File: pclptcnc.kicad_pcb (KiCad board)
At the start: 2 copper layers, 175.3 x 61 mm, 250 parts, among them P1 ARK825A-3, P3 ARK825A-4, P4 ARK825A-3, P5 ARK825A-3, P6 ARK825A-3, P7 ARK825A-3, P8 ARK825A-3, Q1 BC807-40, Q10 BC807-40, Q11 BC807-40, Q12 BC807-40, Q13 BC807-40, Q14 BC807-40, Q15 BC807-40, Q16 BC807-40, Q17 BC807-40, Q18 BC807-40, Q2 BC807-40, Q3 BC807-40, Q4 BC807-40, Q5 BC807-40, Q6 BC807-40, Q7 BC807-40, Q8 BC807-40, Q9 BC807-40, U1 74LVC1G3157GW, U10 SN74LVC2G17, U11 74HCT14, U12 SN74LVC2G17, U13 74HCT14, U2 HCPL2630, U3 HCPL2630, U4 HCPL2630, U5 HCPL2630, U6 HCPL2630, U7 HCPL2630, U8 74HCT14, U9 74HCT14, j1 DB25, j2 DB25

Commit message: working on
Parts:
- CU1: moved to B.Cu
- moved H3 64.8 mm to (-15.4, 89.5)
- moved C2 54.4 mm to (-1.02, 49.1)
- moved C3 54.4 mm to (-4.95, 49.1)
- moved C4 54.4 mm to (-2.98, 49.1)
- moved D1 54.4 mm to (-6.92, 49.1)
- moved R_LED2 54.4 mm to (-6.92, 45.8)
- moved H4 53.7 mm to (215.7, 75.6)
- moved C7 53.0 mm to (-2.10, 102.0)
- moved C8 53.0 mm to (-0.13, 102.0)
- moved C6 53.0 mm to (-4.06, 102.0)
- moved D14 53.0 mm to (-6.03, 102.0)
- moved R_LED15 53.0 mm to (-6.03, 98.6)
- moved F2 52.0 mm to (16.5, 55.9)
- moved DC/DC1 48.5 mm to (0.00, 64.8), turned to 270 degrees
- moved P1 45.5 mm to (44.3, 92.1)
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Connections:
- C1 pad 1: VCC -> /ISOLATED_VCC
- C1 pad 2: GND -> /ISOLATED_GND
- C2 pad 1: VCC -> /ISOLATED_VCC
- C2 pad 2: GND -> /ISOLATED_GND
- C3 pad 1: VCC -> /ISOLATED_VCC
- C3 pad 2: GND -> /ISOLATED_GND
- C4 pad 1: VCC -> /ISOLATED_VCC
- C4 pad 2: GND -> /ISOLATED_GND
- C5 pad 1: /ISOLATED_VCC -> VCC
- C5 pad 2: /ISOLATED_GND -> GND
- C6 pad 1: /ISOLATED_VCC -> VCC
- C6 pad 2: /ISOLATED_GND -> GND
- C7 pad 1: /ISOLATED_VCC -> VCC
- C7 pad 2: /ISOLATED_GND -> GND
- C8 pad 1: /ISOLATED_VCC -> VCC
- C8 pad 2: /ISOLATED_GND -> GND
- D1 pad 1: VCC -> /ISOLATED_VCC
- D14 pad 1: /ISOLATED_VCC -> VCC
- DC/DC1 pad 5: /ISOLATED_GND -> GND
- DC/DC1 pad 7: /ISOLATED_VCC_NFused -> /VCC_NFused
- F1 pad 1: /VCC_NFused -> /ISOLATED_VCC_NFused
- F1 pad 2: VCC -> /ISOLATED_VCC
- F2 pad 1: /ISOLATED_VCC_NFused -> /VCC_NFused
- F2 pad 2: /ISOLATED_VCC -> VCC
- P1 pad 1: /VCC_NFused -> /ISOLATED_VCC_NFused
- P1 pad 3: GND -> /ISOLATED_GND
- R_LED15 pad 1: /ISOLATED_GND -> GND
- R_LED2 pad 2: GND -> /ISOLATED_GND
- TVS1 pad 1: GND -> /ISOLATED_GND
- TVS1 pad 2: VCC -> /ISOLATED_VCC
- TVS2 pad 1: /ISOLATED_GND -> GND
- TVS2 pad 2: /ISOLATED_VCC -> VCC
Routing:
- net GND: track 472.9 -> 56.7 mm, vias 42 -> 7
- net VCC: track 314.8 -> 219.3 mm, vias 11 -> 10
- net /PC8: track 57.7 -> 6.46 mm
- net /PC5: track 53.3 -> 4.42 mm
- net /PC10: track 37.4 -> 21.9 mm
- net /PC7: track 18.6 -> 3.28 mm
- net /PC4: track 16.4 -> 2.27 mm
- net /PC3: track 15.6 -> 1.76 mm
- net /ISOLATED_GND: track 36.8 -> 24.2 mm
- net /PC6: track 14.6 -> 2.39 mm
- net /PC1: track 13.3 -> 2.81 mm
- net /PC2: track 18.2 -> 8.56 mm
- net /PC_OUT_A6: track 73.5 -> 64.6 mm
- net /PC_OUT_A9: track 56.9 -> 50.0 mm
- net /PC_OUT_A5: track 71.9 -> 66.7 mm
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- removed copper zone on F.Cu, net /ISOLATED_VCC
- removed copper zone on F.Cu, net /ISOLATED_VCC_NFused
- removed copper zone on F.Cu, net /VCC_NFused
- removed copper zone on F.Cu, net VCC
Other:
- board size 175.3 x 61 mm -> 174.8 x 59.1 mm

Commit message: regular
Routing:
- net /PC2: track 8.56 -> 1.38 mm
- net VCC: track 219.3 -> 215.9 mm
- net /PC_OUT_A8: track 59.4 -> 56.2 mm
- net /PC_OUT_A7: track 63.7 -> 61.3 mm
- net /PC_OUT_A3: track 2.79 -> 4.80 mm
- net /PC_OUT_A11: track 2.79 -> 4.75 mm
- net /PC_OUT_A2: track 2.79 -> 4.70 mm
- net /PC1: track 2.81 -> 1.38 mm
- net /PC_OUT_A4: track 67.1 -> 65.9 mm
- net /PC_OUT_A5: track 66.7 -> 65.7 mm
- net /PC_OUT_A6: track 64.6 -> 65.6 mm
- net /PC4: track 2.27 -> 1.38 mm

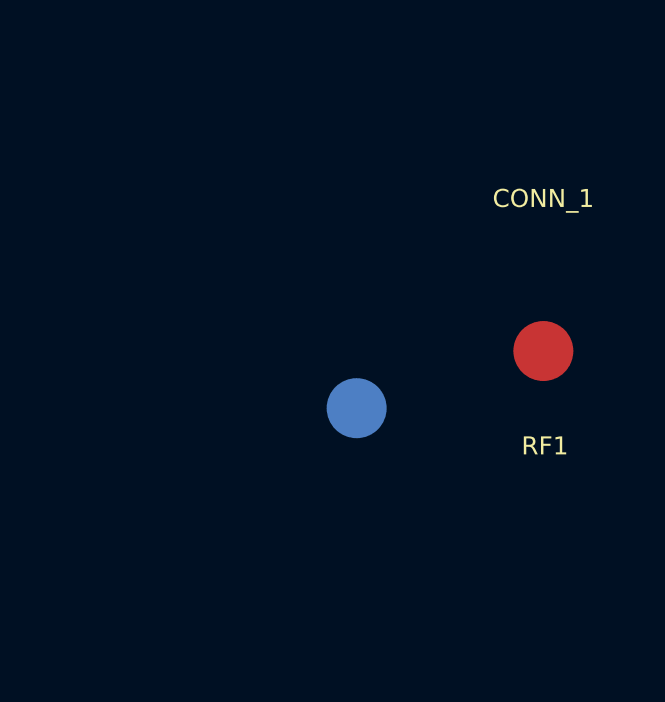
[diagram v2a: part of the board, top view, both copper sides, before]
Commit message: merged all libraries
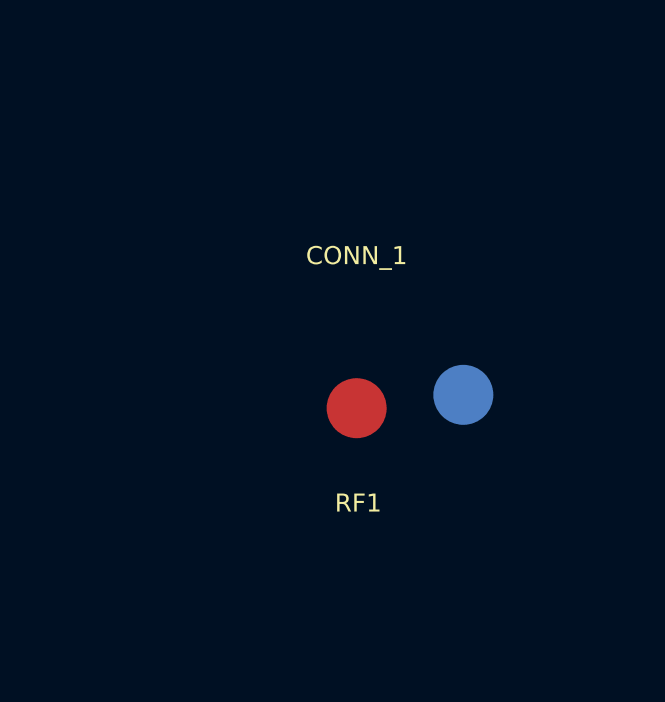
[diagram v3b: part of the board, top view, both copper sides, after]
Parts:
- moved RF1 6.51 mm to (222.1, 52.7)
- moved RF1 3.58 mm to (225.6, 52.3)
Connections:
- DC/DC1 pad 7: /VCC_NFused -> (no net)
- MUX1 pad 10: /PC4 -> (no net)
- MUX1 pad 11: /RC4 -> /PC4
- MUX1 pad 13: /PC3 -> (no net)
- MUX1 pad 14: /RC3 -> (no net)
- MUX1 pad 2: /RC2 -> (no net)
- MUX1 pad 3: /PC2 -> (no net)
- MUX2 pad 10: /PC8 -> (no net)
- MUX2 pad 11: /RC8 -> /PC8
- MUX2 pad 13: /PC7 -> (no net)
- MUX2 pad 14: /RC7 -> (no net)
- MUX2 pad 2: /RC6 -> (no net)
- MUX2 pad 3: /PC6 -> (no net)
- MUX3 pad 10: /PC12 -> (no net)
- MUX3 pad 11: /RC12 -> /PC12
- MUX3 pad 13: /PC10 -> (no net)
- MUX3 pad 14: /RC10 -> (no net)
- MUX3 pad 2: /RC9 -> (no net)
- MUX3 pad 3: /PC9 -> (no net)
- MUX4 pad 10: GND -> (no net)
- MUX4 pad 11: /SENSOR_1 -> GND
- MUX4 pad 13: GND -> (no net)
- MUX4 pad 14: /SENSOR_2 -> (no net)
- MUX4 pad 2: /SENSOR_4 -> (no net)
- MUX4 pad 3: GND -> (no net)
- P1 pad 1: /ISOLATED_VCC_NFused -> (no net)
- U11 pad 12: /PC3 -> (no net)
- U11 pad 4: /PC7 -> (no net)
- U11 pad 6: /PC6 -> (no net)
- U11 pad 8: /PC2 -> (no net)
- U12 pad 6: /PC10 -> (no net)
- U13 pad 2: /PC9 -> (no net)
- U8 pad 12: /RC9 -> (no net)
- U8 pad 2: /RC10 -> (no net)
- U8 pad 4: /RC8 -> (no net)
- U8 pad 8: /RC12 -> (no net)
- U9 pad 10: /RC7 -> (no net)
- U9 pad 12: /RC4 -> (no net)
- U9 pad 4: /RC3 -> (no net)
- U9 pad 6: /RC2 -> (no net)
- U9 pad 8: /RC6 -> (no net)
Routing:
- net (no net): track 0.27 -> 163.8 mm, vias 1 -> 9
- net /PC9: track 28.1 -> 0.00 mm, vias 1 -> 0
- net /RC4: track 24.2 -> 0.00 mm
- net /RC12: track 23.7 -> 0.00 mm
- net /PC12: track 31.5 -> 55.2 mm
- net /PC4: track 1.38 -> 24.2 mm, vias 1 -> 0
- net /RC10: track 22.6 -> 0.00 mm
- net /PC10: track 21.9 -> 0.00 mm, vias 1 -> 0
- net /RC3: track 21.9 -> 0.00 mm
- net GND: track 56.7 -> 74.0 mm
- net /SENSOR_1: track 139.6 -> 122.4 mm
- net /RC2: track 17.1 -> 0.00 mm
- net /RC8: track 13.4 -> 0.00 mm
- net /RC7: track 13.0 -> 0.00 mm
- net /RC9: track 11.6 -> 0.00 mm
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
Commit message: futher library development
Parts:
- moved R88 12.7 mm to (178.8, 43.6), turned to 0 degrees
- moved MUX4 11.7 mm to (184.7, 48.1), turned to 90 degrees
- moved R82 7.93 mm to (178.8, 45.5), turned to 0 degrees
- moved R86 7.33 mm to (178.8, 47.4), turned to 0 degrees
- moved R90 3.92 mm to (178.8, 49.3), turned to 0 degrees
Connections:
- DC/DC1 pad 7: (no net) -> /VCC_NFused
- MUX1 pad 10: (no net) -> /PC4
- MUX1 pad 11: /PC4 -> /RC4
- MUX1 pad 13: (no net) -> /PC3
- MUX1 pad 14: (no net) -> /RC3
- MUX1 pad 2: (no net) -> /RC2
- MUX1 pad 3: (no net) -> /PC2
- MUX2 pad 10: (no net) -> /PC8
- MUX2 pad 11: /PC8 -> /RC8
- MUX2 pad 13: (no net) -> /PC7
- MUX2 pad 14: (no net) -> /RC7
- MUX2 pad 2: (no net) -> /RC6
- MUX2 pad 3: (no net) -> /PC6
- MUX3 pad 10: (no net) -> /PC12
- MUX3 pad 11: /PC12 -> /RC12
- MUX3 pad 13: (no net) -> /PC10
- MUX3 pad 14: (no net) -> /RC10
- MUX3 pad 2: (no net) -> /RC9
- MUX3 pad 3: (no net) -> /PC9
- MUX4 pad 10: (no net) -> GND
- MUX4 pad 11: GND -> /SENSOR_1
- MUX4 pad 13: (no net) -> GND
- MUX4 pad 14: (no net) -> /SENSOR_2
- MUX4 pad 2: (no net) -> /SENSOR_4
- MUX4 pad 3: (no net) -> GND
- P1 pad 1: (no net) -> /ISOLATED_VCC_NFused
- U11 pad 12: (no net) -> /PC3
- U11 pad 4: (no net) -> /PC7
- U11 pad 6: (no net) -> /PC6
- U11 pad 8: (no net) -> /PC2
- U12 pad 6: (no net) -> /PC10
- U13 pad 2: (no net) -> /PC9
- U8 pad 12: (no net) -> /RC9
- U8 pad 2: (no net) -> /RC10
- U8 pad 4: (no net) -> /RC8
- U8 pad 8: (no net) -> /RC12
- U9 pad 10: (no net) -> /RC7
- U9 pad 12: (no net) -> /RC4
- U9 pad 4: (no net) -> /RC3
- U9 pad 6: (no net) -> /RC2
- U9 pad 8: (no net) -> /RC6
- j2 pad 10: /PC_IN1 -> /PC_IN3
- j2 pad 12: /PC_IN3 -> /PC_IN1
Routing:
- net (no net): track 163.8 -> 0.27 mm, vias 9 -> 1
- net /SENSOR_2: track 130.9 -> 95.4 mm
- net GND: track 74.0 -> 44.8 mm, vias 7 -> 3
- net /PC9: track 0.00 -> 28.1 mm, vias 0 -> 1
- net /SENSOR_3: track 113.3 -> 87.5 mm
- net /SENSOR_1: track 122.4 -> 97.2 mm
- net /RC4: track 0.00 -> 24.2 mm
- net /RC12: track 0.00 -> 23.7 mm
- net /PC12: track 55.2 -> 31.5 mm
- net /PC4: track 24.2 -> 1.38 mm, vias 0 -> 1
- net /RC10: track 0.00 -> 22.6 mm
- net /PC10: track 0.00 -> 21.9 mm, vias 0 -> 1
- net /RC3: track 0.00 -> 21.9 mm
- net /SENSOR_5: track 107.2 -> 88.5 mm
- net /SENSOR_4: track 106.5 -> 89.0 mm
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
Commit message: 05.11.1305.11.1305.11.1305.11.1305.11.13
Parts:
- moved D14 72.0 mm to (46.2, 52.5), turned to 270 degrees
- moved CU4 69.6 mm to (75.6, 59.2)
- moved C6 69.2 mm to (47.9, 56.3), turned to 270 degrees
- moved C7 69.1 mm to (49.7, 56.3), turned to 270 degrees
- moved C8 68.9 mm to (51.5, 56.3), turned to 270 degrees
- moved R_LED15 67.2 mm to (46.2, 56.3), turned to 90 degrees
- moved TVS2 51.6 mm to (39.6, 55.0), turned to 90 degrees
- moved TVS1 50.3 mm to (52.5, 72.2), turned to 270 degrees
- moved CU5 50.3 mm to (73.7, 59.2)
- moved DC/DC1 45.5 mm to (45.0, 71.6), turned to 90 degrees
- moved C5 44.5 mm to (57.7, 53.3), turned to 90 degrees
- moved C1 36.2 mm to (57.8, 70.3), turned to 270 degrees
- moved F2 35.6 mm to (50.2, 44.4)
- moved F1 35.0 mm to (50.2, 80.2)
- moved CU12 34.8 mm to (71.8, 59.2), turned to 90 degrees
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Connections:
- MUX4 pad 14: /SENSOR_2 -> /SENSOR_3
- MUX4 pad 5: /SENSOR_3 -> /SENSOR_2
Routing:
- net /PC/RC_SW: track 182.7 -> 61.2 mm, vias 4 -> 6
- net (no net): track 0.27 -> 37.9 mm
- net /SENSOR_1: track 97.2 -> 130.0 mm, vias 1 -> 2
- net /SENSOR_3: track 87.5 -> 120.1 mm, vias 1 -> 2
- net /PC12: track 31.5 -> 57.4 mm
- net /SENSOR_2: track 95.4 -> 120.2 mm, vias 1 -> 2
- net /SENSOR_5: track 88.5 -> 110.9 mm, vias 1 -> 2
- net /PC_OUT12: track 25.2 -> 2.79 mm
- net /SENSOR_4: track 89.0 -> 111.1 mm, vias 1 -> 2
- net /SRC_SEL: track 61.4 -> 81.6 mm
- net /PC9: track 28.1 -> 12.1 mm
- net VCC: track 206.5 -> 221.9 mm, vias 10 -> 9
- net /IOSRCLED_R: track 4.70 -> 19.7 mm
- net /PC11: track 30.3 -> 16.2 mm
- net /PC_IN4: track 53.9 -> 64.7 mm
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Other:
- net class power removed
- rule pad_to_mask_clearance: 0.05 -> 0

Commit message: huge optocouplers movement
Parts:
- moved H3 55.0 mm to (34.6, 45.6)
- moved CU3 54.0 mm to (15.7, 58.9)
- moved CU5 54.0 mm to (19.7, 58.9)
- moved CU12 54.0 mm to (17.7, 58.9)
- moved CU13 54.0 mm to (13.7, 58.9)
- moved CU4 54.0 mm to (21.6, 58.9)
- moved H2 50.9 mm to (33.4, 76.7)
- moved CU2 42.3 mm to (23.5, 58.9)
- moved R_LED2 34.5 mm to (48.7, 64.1), turned to 0 degrees
- moved D1 33.9 mm to (48.1, 66.7)
- moved C3 33.8 mm to (50.0, 66.7)
- moved C4 33.7 mm to (51.9, 66.7)
- moved C2 33.7 mm to (53.8, 66.7)
- moved RF2 31.0 mm to (32.8, 60.5)
- moved RF2 28.0 mm to (32.8, 60.5)
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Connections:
- DC/DC1 pad 1: VCC -> /ISOLATED_VCC
- DC/DC1 pad 2: GND -> /ISOLATED_GND
- MUX1 pad 11: /RC4 -> /RC1
- MUX1 pad 12: /FLTRD_SGNL2 -> /FLTRD_SGNL3
- MUX1 pad 13: /PC3 -> /PC1
- MUX1 pad 14: /RC3 -> /RC2
- MUX1 pad 2: /RC2 -> /RC4
- MUX1 pad 4: /FLTRD_SGNL1 -> /FLTRD_SGNL4
- MUX1 pad 5: /RC1 -> /RC3
- MUX1 pad 6: /PC1 -> /PC3
- MUX1 pad 7: /FLTRD_SGNL3 -> /FLTRD_SGNL2
- MUX1 pad 9: /FLTRD_SGNL4 -> /FLTRD_SGNL1
- MUX2 pad 10: /PC8 -> /PC12
- MUX2 pad 11: /RC8 -> /RC11
- MUX2 pad 5: /RC5 -> /RC9
- MUX3 pad 10: /PC12 -> /PC10
- MUX3 pad 11: /RC12 -> /RC10
- MUX3 pad 13: /PC10 -> /PC11
- MUX3 pad 14: /RC10 -> /RC12
- MUX3 pad 2: /RC9 -> /RC5
- MUX3 pad 5: /RC11 -> /RC8
- MUX3 pad 6: /PC11 -> /PC8
- U11 pad 13: /PC_OUT_A7 -> /PC_OUT_A9
- U11 pad 9: /PC_OUT_A9 -> /PC_OUT_A7
- U13 pad 2: /PC9 -> /PC8
- U13 pad 4: /PC8 -> /PC9
- U8 pad 1: /RCOUT4 -> /RCOUT3
- U8 pad 11: /RCOUT2 -> /RCOUT5
- U8 pad 13: /RCOUT3 -> /RCOUT6
- U8 pad 3: /RCOUT5 -> /RCOUT2
- U8 pad 5: /RCOUT6 -> /RCOUT1
- U8 pad 9: /RCOUT1 -> /RCOUT4
- U9 pad 1: /RCOUT10 -> /RCOUT12
- U9 pad 5: /RCOUT12 -> /RCOUT10
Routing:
- net VCC: track 221.9 -> 159.4 mm, vias 9 -> 7
- net (no net): track 37.9 -> 0.00 mm, vias 1 -> 0
- net GND: track 50.3 -> 14.4 mm, vias 5 -> 2
- net /PC5: track 6.67 -> 37.3 mm, vias 1 -> 0
- net /RCOUT3: track 39.1 -> 15.7 mm
- net /FLTRD_SGNL9: track 19.6 -> 0.00 mm
- net /FLTRD_SGNL5: track 19.6 -> 0.00 mm
- net N-00000169: track 3.22 -> 21.9 mm
- net /RCOUT2: track 34.0 -> 15.5 mm
- net /FLTRD_SGNL1: track 20.1 -> 2.16 mm
- net /RCOUT10: track 26.6 -> 9.87 mm
- net /PC12: track 57.4 -> 73.7 mm, vias 0 -> 1
- net /PC11: track 16.2 -> 32.3 mm
- net /PC8: track 9.33 -> 25.2 mm
- net /RC4: track 24.2 -> 8.44 mm
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
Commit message: близкая компоновка
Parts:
- moved R91 12.4 mm to (194.1, 78.1)
- moved R27 11.5 mm to (100.1, 65.2)
- moved R99 10.4 mm to (189.0, 78.1)
- moved R107 8.74 mm to (184.0, 78.1)
- moved R69 8.61 mm to (150.0, 65.8), turned to 0 degrees
- moved R92 7.55 mm to (178.9, 78.1)
- moved OPTOCPLR1 7.18 mm to (194.1, 75.6)
- moved OPTOCPLR4 7.18 mm to (173.8, 75.6)
- moved OPTOCPLR5 7.18 mm to (184.0, 75.6)
- moved OPTOCPLR2 7.18 mm to (178.9, 75.6)
- moved OPTOCPLR3 7.18 mm to (189.0, 75.6)
- moved R100 7.11 mm to (173.8, 78.1)
- moved P3 6.35 mm to (67.1, 85.7)
- moved P4 6.35 mm to (97.6, 85.7)
- moved P5 6.35 mm to (120.5, 85.7)
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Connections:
- MUX2 pad 11: /RC11 -> /RC7
- MUX2 pad 12: /FLTRD_SGNL6 -> /FLTRD_SGNL7
- MUX2 pad 13: /PC7 -> /PC5
- MUX2 pad 14: /RC7 -> /RC6
- MUX2 pad 2: /RC6 -> /RC11
- MUX2 pad 3: /PC6 -> /PC7
- MUX2 pad 4: /FLTRD_SGNL5 -> /FLTRD_SGNL8
- MUX2 pad 6: /PC5 -> /PC6
- MUX2 pad 7: /FLTRD_SGNL7 -> /FLTRD_SGNL6
- MUX2 pad 9: /FLTRD_SGNL8 -> /FLTRD_SGNL5
- MUX3 pad 7: /FLTRD_SGNL11 -> /FLTRD_SGNL12
- MUX3 pad 9: /FLTRD_SGNL12 -> /FLTRD_SGNL11
- U10 pad 4: /PC12 -> /PC4
- U11 pad 2: /PC4 -> /PC6
- U11 pad 6: /PC6 -> /PC12
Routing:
- net VCC: track 159.4 -> 275.5 mm, vias 7 -> 9
- net /PC/RC_SW: track 60.8 -> 144.8 mm, vias 3 -> 5
- net /PC4: track 12.7 -> 90.8 mm, vias 1 -> 2
- net /ISOLATED_GND: track 22.2 -> 99.3 mm
- net /PC12: track 73.7 -> 10.0 mm
- net /ISOLATED_VCC: track 559.1 -> 620.7 mm
- net GND: track 14.4 -> 65.9 mm, vias 2 -> 6
- net /FLTRD_SGNL9: track 0.00 -> 36.1 mm
- net /RC6: track 0.00 -> 21.1 mm
- net /RC7: track 0.00 -> 20.4 mm
- net /FLTRD_SGNL8: track 0.00 -> 18.4 mm
- net /PC3: track 8.47 -> 25.1 mm
- net /ISOLATED_VCC_NFused: track 0.00 -> 15.0 mm
- net /PC5: track 37.3 -> 50.9 mm, vias 0 -> 1
- net /PC1: track 11.3 -> 23.6 mm
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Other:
- board outline removed

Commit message: version 0.2a completed
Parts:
- removed R1: 2K7, SM0805
- C1, C5: footprint c_elec_10x10 -> c_elec_8x10.5
- CU4, CU5: moved to B.Cu
- F1, F2: footprint FUSE5-20_1.4mm -> FUSE_HOLDER
- moved CU4 159.9 mm to (181.4, 53.0), turned to 270 degrees
- moved CU5 153.6 mm to (173.3, 61.1)
- moved CU3 116.4 mm to (132.0, 64.5), turned to 270 degrees
- moved CU12 100.5 mm to (118.2, 57.9), turned to 0 degrees
- moved CU2 92.0 mm to (115.4, 63.6), turned to 270 degrees
- moved CU13 77.7 mm to (91.4, 56.7)
- moved CU15 71.9 mm to (95.6, 59.8), turned to 270 degrees
- moved CU1 65.2 mm to (86.5, 63.6), turned to 0 degrees
- moved TVS1 25.0 mm to (40.7, 78.9), turned to 90 degrees
- moved CU14 21.7 mm to (149.0, 45.1), turned to 90 degrees
- moved H2 17.1 mm to (33.7, 88.9)
- moved CU16 16.9 mm to (167.4, 62.5), turned to 90 degrees
- moved P1 15.2 mm to (59.5, 85.7), turned to 180 degrees
- moved CU17 12.7 mm to (160.8, 63.4), turned to 180 degrees
- moved F1 11.5 mm to (63.3, 73.0), turned to 180 degrees
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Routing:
- net GND: track 65.9 -> 391.3 mm, vias 6 -> 42
- net VCC: track 275.5 -> 395.6 mm, vias 9 -> 10
- net /ISOLATED_GND: track 99.3 -> 24.8 mm, vias 0 -> 1
- net /FLTRD_SGNL1: track 2.16 -> 9.87 mm
- net /VCC_NFused: track 6.88 -> 0.00 mm
- net N-00000138: track 8.74 -> 2.48 mm
- net /ISOLATED_VCC: track 620.7 -> 626.3 mm
- net N-00000174: track 21.9 -> 17.5 mm
- net /FLTRD_SGNL3: track 7.19 -> 11.1 mm
- net /IOSRCTR_BASE: track 4.56 -> 1.69 mm
- net N-00000137: track 8.90 -> 6.82 mm
- net /FLTRD_SGNL2: track 4.28 -> 5.48 mm
- net /OUTPUT_SIGNAL9: track 14.8 -> 13.8 mm
- net /OUTPUT_SIGNAL8: track 14.6 -> 13.6 mm
- net /OUTPUT_SIGNAL7: track 15.4 -> 14.4 mm
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- added copper zone on F.Cu, net /ISOLATED_VCC
- added copper zone on F.Cu, net /VCC_NFused
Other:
- board outline added: 180.5 x 52.3 mm
